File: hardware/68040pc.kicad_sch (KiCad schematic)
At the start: 3 parts, among them P8 Conn_01x06, P9 Conn_01x06, U1 68LC040

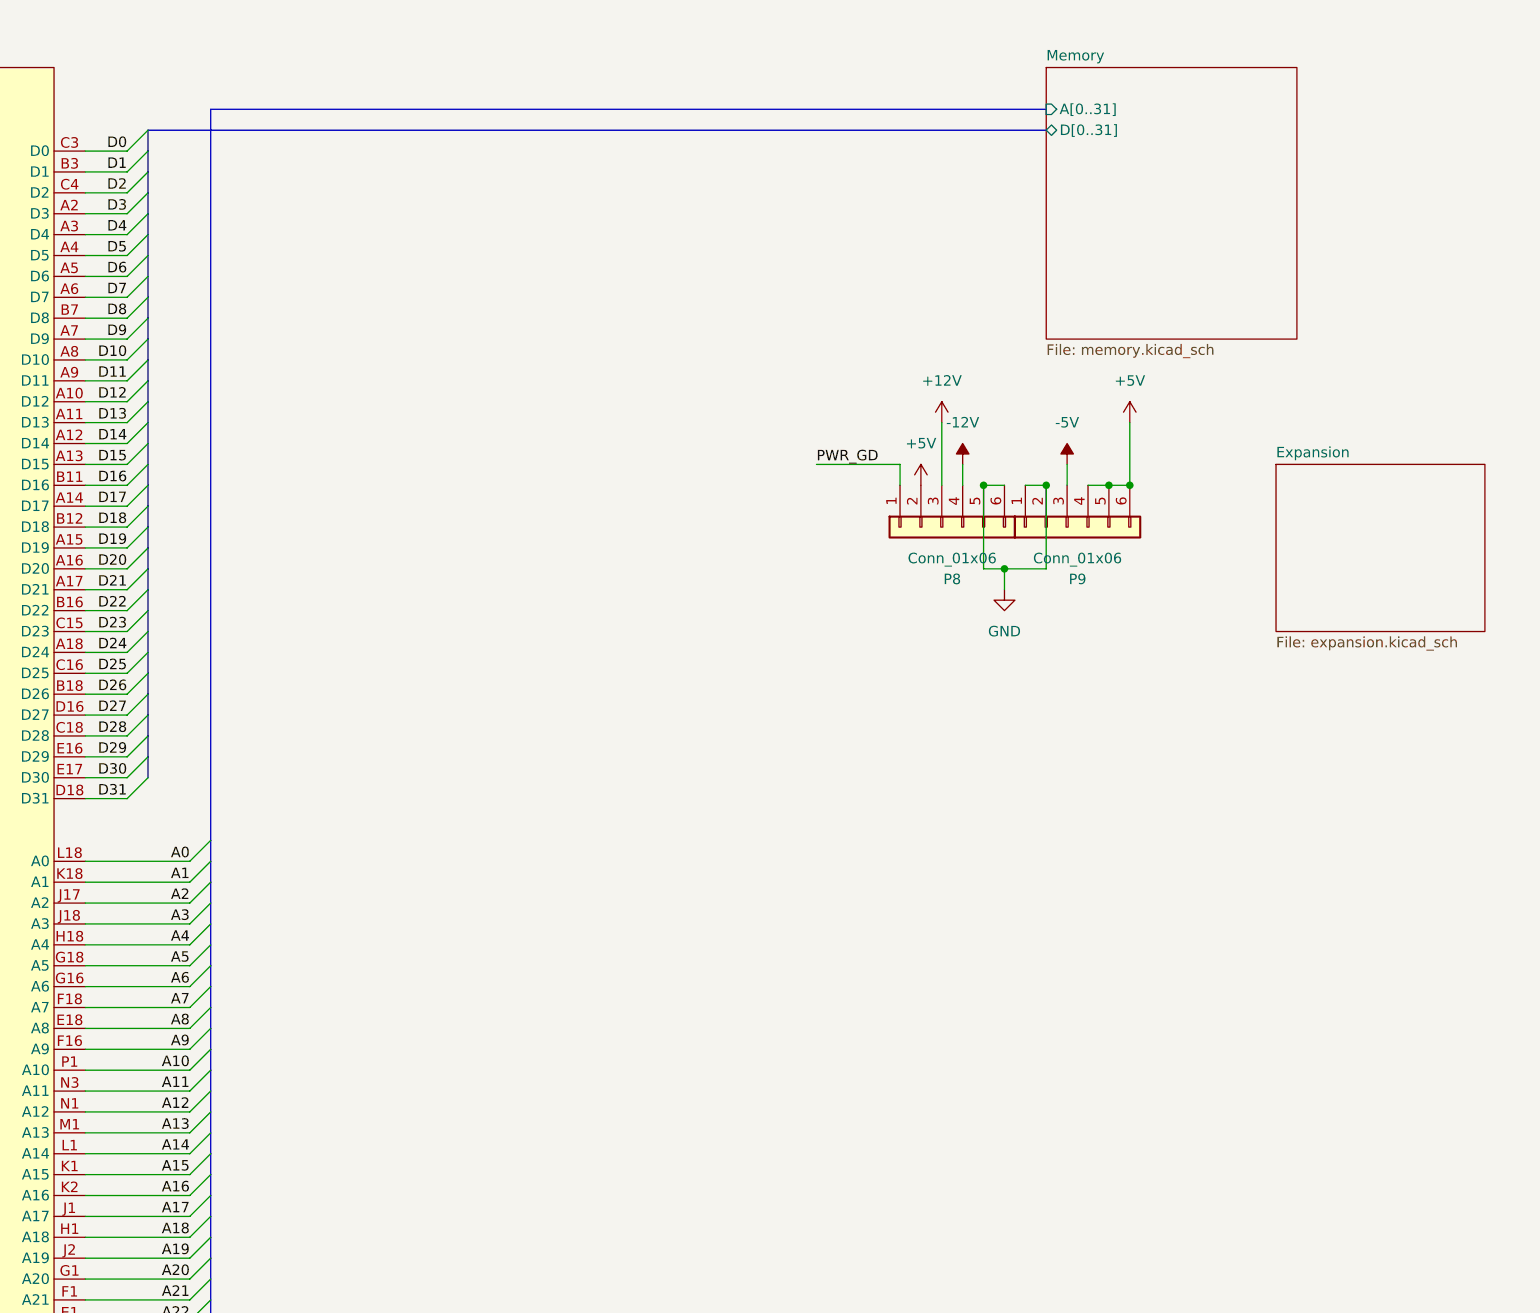
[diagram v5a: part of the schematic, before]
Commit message: reconfigure expansion slot schematic
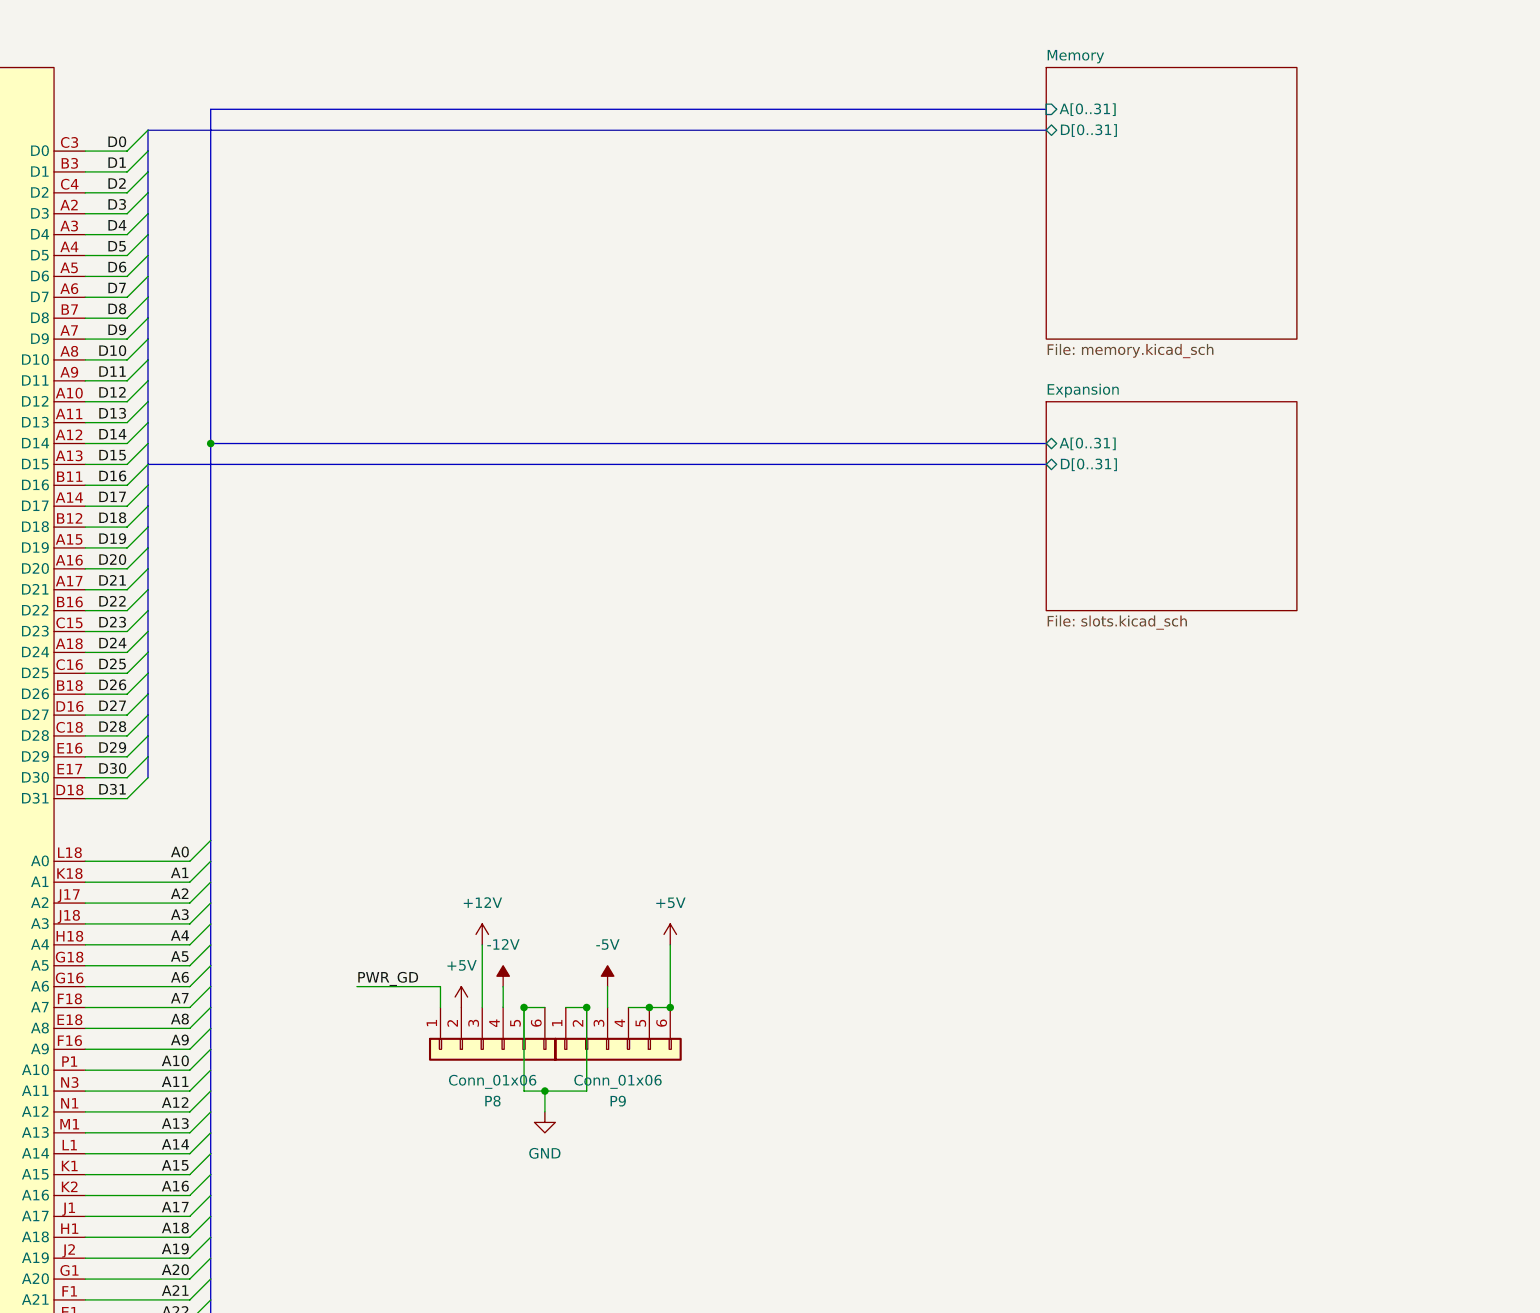
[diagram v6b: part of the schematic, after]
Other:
- sheet Expansion: file expansion.kicad_sch -> slots.kicad_sch
- sheet Expansion ports: added A[0..31], D[0..31]; removed none
- moved on the sheet: P8, P9

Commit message: updates
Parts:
- removed P8, P9: Conn_01x06, 68040:15-48-0106, symbol Connector_Generic:Conn_01x06
- added U8: LTC6905xS5-133, Package_TO_SOT_SMD:TSOT-23-5, symbol Oscillator:LTC6905xS5-133
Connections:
- net ~{TA}: no longer U1.T14 (~{TA})
- net ~{TBI}: no longer U1.S11 (~{TBI})
- net ~{TCI}: no longer U1.T10 (~{TCI})
- net ~{TEA}: no longer U1.S13 (~{TEA})
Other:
- added sheet Power (power.kicad_sch)
- sheet Expansion ports: added ~{EXP_OE}; removed none

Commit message: updates
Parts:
- added R4: 10k, Resistor_SMD:R_0603_1608Metric, symbol Device:R_Small_US
- added R5: 10k, Capacitor_SMD:C_0603_1608Metric, symbol Device:R_Small_US
- added U23: PCF8584, Package_SO:SOIC-20W_7.5x12.8mm_P1.27mm, symbol Interface_Expansion:PCF8584
- added U24: ~, Package_LCC:PLCC-68_SMD-Socket, symbol 68040:MC68150
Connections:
- net A0: now also U24.20 (A0)
- net A1: now also U24.19 (A1)
- net BCLK: now also U24.24 (BCLK)
- net D0: now also U23.7 (D0), U24.53 (D0)
- net D1: now also U23.8 (D1), U24.54 (D1)
- net D10: now also U24.63 (D10)
- net D11: now also U24.64 (D11)
- net D12: now also U24.65 (D12)
- net D13: now also U24.66 (D13)
- net D14: now also U24.67 (D14)
- net D15: now also U24.68 (D15)
- net D16: now also U24.2 (D16)
- net D17: now also U24.3 (D17)
- net D18: now also U24.4 (D18)
- net D19: now also U24.5 (D19)
- net D2: now also U23.9 (D2), U24.55 (D2)
- net D20: now also U24.6 (D20)
- net D21: now also U24.7 (D21)
- net D22: now also U24.8 (D22)
- net D23: now also U24.9 (D23)
- net D24: now also U24.10 (D24)
- net D25: now also U24.11 (D25)
- net D26: now also U24.12 (D26)
- net D27: now also U24.13 (D27)
- net D28: now also U24.14 (D28)
- net D29: now also U24.15 (D29)
- net D3: now also U23.11 (D3), U24.56 (D3)
- net D30: now also U24.16 (D30)
- net D31: now also U24.17 (D31)
- net D4: now also U23.12 (D4), U24.57 (D4)
- net D5: now also U23.13 (D5), U24.58 (D5)
- net D6: now also U23.14 (D6), U24.59 (D6)
- net D7: now also U23.15 (D7), U24.60 (D7)
- net D8: now also U24.61 (D8)
- net D9: now also U24.62 (D9)
- net R/~{W}: now also U24.23 (R/~{W})
- net SIZ0: now also U24.22 (SIZ0)
- net SIZ1: now also U24.21 (SIZ1)
- net ~{TA}: now also U24.26 (~{TA})
- net +3.3V: now reaches U8.1 (VDD)
- net +3.3V: now also U8.3 (OE), U8.4 (DIV)
- net GND: now reaches U8.2 (GND)
- net GND: now also U23.10 (VSS), U24.18 (GND), U24.52 (GND)
- net SYS_CLK: now reaches U8.5 (OUT)
- new net +5V: U23.20 (VDD), U24.1 (V_{CC}), U24.35 (V_{CC})
- new net I2C_SCL: R4.2, U23.2 (SDA)
- new net I2C_SDA: R5.2, U23.3 (SCL)
- new net PA0: U23.6 (A0), U24.33 (PA0)
- new net PA1: U24.34 (PA1)
- new net ~{68150_CS}: U24.25 (~{CS})
- new net ~{DSACK0}: U24.29 (~{DSACK1})
- new net ~{DSACK1}: U24.28 (~{DSACK0})
- new net ~{DS}: U24.27 (~{DS})
- new net ~{I2C_DTACK}: U23.16 (~{RD})
- new net ~{I2C_SEL}: U23.17 (~{CS})
- new net ~{LWE}: U24.31 (~{LWE})
- new net ~{SWE}: U23.18 (~{WR}), U24.30 (~{SWE})
- new net ~{UWE}: U24.32 (~{UWE})
